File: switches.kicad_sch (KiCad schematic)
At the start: 140 parts

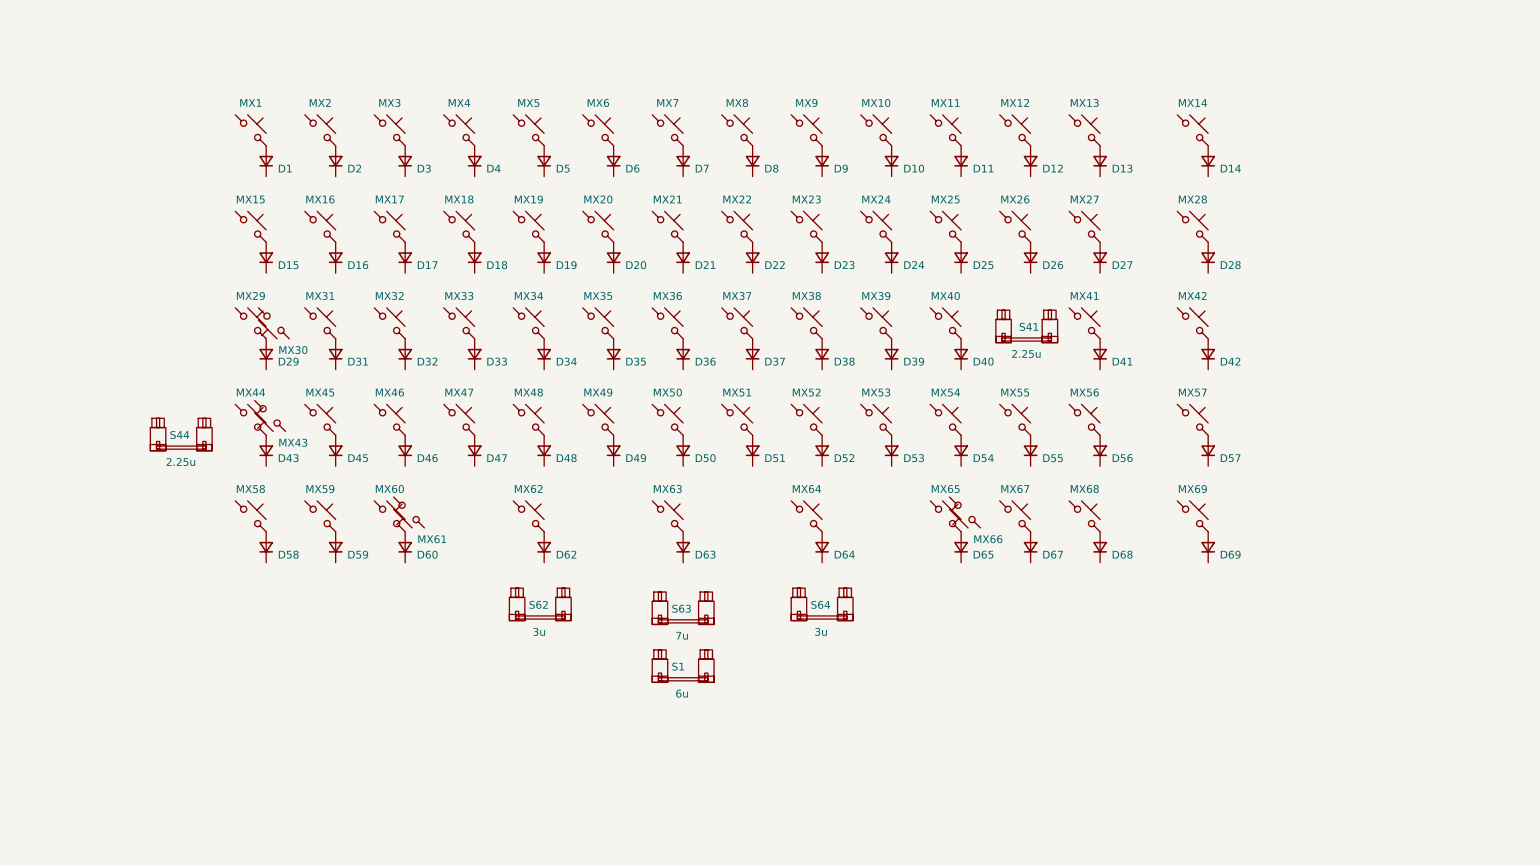
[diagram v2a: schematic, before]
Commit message: Complete matrix and add Skyloong knob module
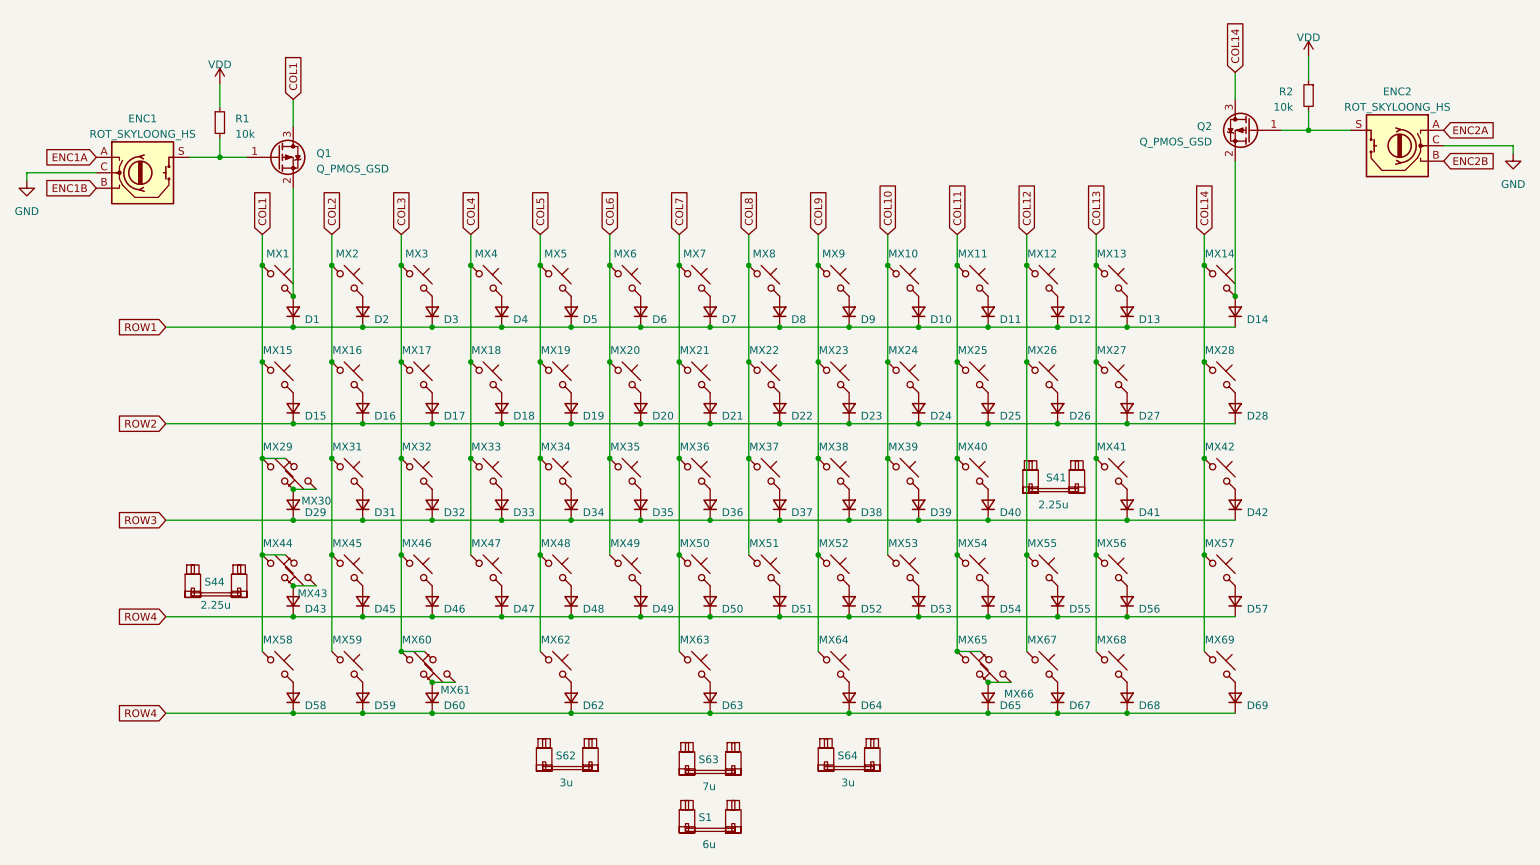
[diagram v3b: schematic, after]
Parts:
- added ENC1, ENC2: ROT_SKYLOONG_HS, PCM_marbastlib-various:ROT_SKYLOONG_HS-Switch, symbol PCM_marbastlib-various:ROT_SKYLOONG_HS-Switch
- added Q1, Q2: Q_PMOS_GSD, Package_TO_SOT_SMD:SOT-23, symbol Device:Q_PMOS_GSD
- added R1, R2: 10k, Resistor_SMD:R_0603_1608Metric, symbol Device:R_Small
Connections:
- net COL14: now reaches MX42.1
- net COL14: now also MX14.1, MX28.1, MX57.1, MX69.1, Q2.3 (D)
- net ROW3: now reaches D35.1 (K)
- net ROW3: now also D29.1 (K), D31.1 (K), D32.1 (K), D33.1 (K), D34.1 (K), D36.1 (K), D37.1 (K), D38.1 (K), D39.1 (K), D40.1 (K), D41.1 (K), D42.1 (K)
- net ROW4: now reaches D52.1 (K)
- net ROW4: now also D43.1 (K), D45.1 (K), D46.1 (K), D47.1 (K), D48.1 (K), D49.1 (K), D50.1 (K), D51.1 (K), D53.1 (K), D54.1 (K), D55.1 (K), D56.1 (K), D57.1 (K), D58.1 (K), D59.1 (K), D60.1 (K), D62.1 (K), D63.1 (K), D64.1 (K), D65.1 (K), D67.1 (K), D68.1 (K), D69.1 (K)
- net ROW1: now reaches D3.1 (K)
- net ROW1: now also D1.1 (K), D10.1 (K), D11.1 (K), D12.1 (K), D13.1 (K), D14.1 (K), D2.1 (K), D4.1 (K), D5.1 (K), D6.1 (K), D7.1 (K), D8.1 (K), D9.1 (K)
- net ROW2: now reaches D15.1 (K)
- net ROW2: now also D16.1 (K), D17.1 (K), D18.1 (K), D19.1 (K), D20.1 (K), D21.1 (K), D22.1 (K), D23.1 (K), D24.1 (K), D25.1 (K), D26.1 (K), D27.1 (K), D28.1 (K)
- net COL3: now reaches MX3.1
- net COL3: now also MX17.1, MX32.1, MX46.1, MX60.1, MX61.2
- net COL10: now reaches MX10.1
- net COL10: now also MX24.1, MX39.1, MX53.1
- net COL2: now reaches MX45.1
- net COL2: now also MX16.1, MX2.1, MX31.1, MX59.1
- net at D14.2 (A), MX14.2: now also Q2.2 (S)
- net COL5: now reaches MX19.1
- net COL5: now also MX34.1, MX48.1, MX5.1, MX62.1
- net at D1.2 (A), MX1.2: now also Q1.2 (S)
- net COL11: now reaches MX11.1
- net COL11: now also MX25.1, MX40.1, MX54.1, MX65.1, MX66.2
- net COL4: now reaches MX18.1
- net COL4: now also MX33.1, MX4.1, MX47.1
- net COL8: now reaches MX22.1
- net COL8: now also MX37.1, MX51.1, MX8.1
- net COL1: now reaches MX1.1
- net COL1: now also MX15.1, MX29.1, MX30.2, MX43.2, MX44.1, MX58.1, Q1.3 (D)
- net COL12: now reaches MX55.1
- net COL12: now also MX12.1, MX26.1, MX67.1
- net COL6: now reaches MX20.1
- net COL6: now also MX35.1, MX49.1, MX6.1
- net COL13: now reaches MX56.1
- net COL13: now also MX13.1, MX27.1, MX41.1, MX68.1
- net at D60.2 (A), MX60.2: now also MX61.1
- net at D65.2 (A), MX65.2: now also MX66.1
- net at MX30.1: now also D29.2 (A), MX29.2
- net at D43.2 (A), MX44.2: now also MX43.1
- net COL9: now reaches MX23.1
- net COL9: now also MX38.1, MX52.1, MX64.1, MX9.1
- net COL7: now reaches MX63.1
- net COL7: now also MX21.1, MX36.1, MX50.1, MX7.1
- new net: ENC1.S, Q1.1 (G), R1.2
- new net: ENC2.S, Q2.1 (G), R2.2
- new net ENC1A: ENC1.A
- new net ENC1B: ENC1.B
- new net ENC2A: ENC2.A
- new net ENC2B: ENC2.B
- new net GND: ENC1.C, ENC2.C
- new net VDD: R1.1, R2.1
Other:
- moved on the sheet: D1, D10, D11, D12, D13, D14, D15, D16, D17, D18, D19, D2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

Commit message: Complete column traces
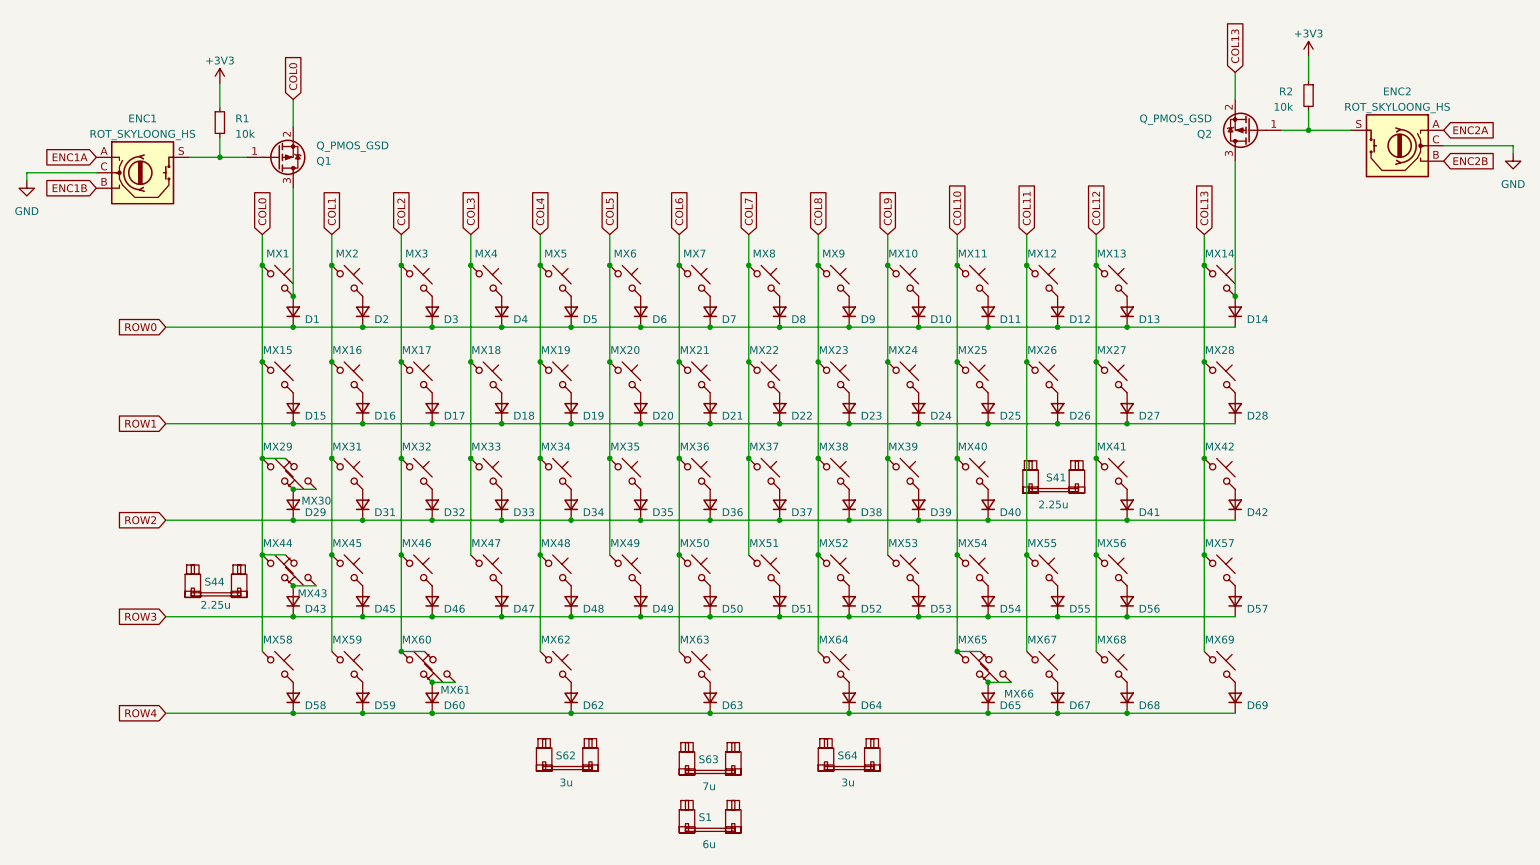
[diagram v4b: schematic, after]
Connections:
- net COL1: now also MX16.1, MX2.1, MX31.1, MX45.1, MX59.1; no longer MX1.1, MX15.1, MX29.1, MX30.2, MX43.2, MX44.1, MX58.1, Q1.3 (D)
- net COL10: now also MX11.1, MX25.1, MX40.1, MX54.1, MX65.1, MX66.2; no longer MX10.1, MX24.1, MX39.1, MX53.1
- net COL11: now also MX12.1, MX26.1, MX55.1, MX67.1; no longer MX11.1, MX25.1, MX40.1, MX54.1, MX65.1, MX66.2
- net COL12: now also MX13.1, MX27.1, MX41.1, MX56.1, MX68.1; no longer MX12.1, MX26.1, MX55.1, MX67.1
- net COL13: now also MX14.1, MX28.1, MX42.1, MX57.1, MX69.1, Q2.2 (S); no longer MX13.1, MX27.1, MX41.1, MX56.1, MX68.1
- net COL2: now also MX17.1, MX3.1, MX32.1, MX46.1, MX60.1, MX61.2; no longer MX16.1, MX2.1, MX31.1, MX45.1, MX59.1
- net COL3: now also MX18.1, MX33.1, MX4.1, MX47.1; no longer MX17.1, MX3.1, MX32.1, MX46.1, MX60.1, MX61.2
- net COL4: now also MX19.1, MX34.1, MX48.1, MX5.1, MX62.1; no longer MX18.1, MX33.1, MX4.1, MX47.1
- net COL5: now also MX20.1, MX35.1, MX49.1, MX6.1; no longer MX19.1, MX34.1, MX48.1, MX5.1, MX62.1
- net COL6: now also MX21.1, MX36.1, MX50.1, MX63.1, MX7.1; no longer MX20.1, MX35.1, MX49.1, MX6.1
- net COL7: now also MX22.1, MX37.1, MX51.1, MX8.1; no longer MX21.1, MX36.1, MX50.1, MX63.1, MX7.1
- net COL8: now also MX23.1, MX38.1, MX52.1, MX64.1, MX9.1; no longer MX22.1, MX37.1, MX51.1, MX8.1
- net COL9: now also MX10.1, MX24.1, MX39.1, MX53.1; no longer MX23.1, MX38.1, MX52.1, MX64.1, MX9.1
- net ROW1: now also D15.1 (K), D16.1 (K), D17.1 (K), D18.1 (K), D19.1 (K), D20.1 (K), D21.1 (K), D22.1 (K), D23.1 (K), D24.1 (K), D25.1 (K), D26.1 (K), D27.1 (K), D28.1 (K); no longer D1.1 (K), D10.1 (K), D11.1 (K), D12.1 (K), D13.1 (K), D14.1 (K), D2.1 (K), D3.1 (K), D4.1 (K), D5.1 (K), D6.1 (K), D7.1 (K), D8.1 (K), D9.1 (K)
- net ROW2: now also D29.1 (K), D31.1 (K), D32.1 (K), D33.1 (K), D34.1 (K), D35.1 (K), D36.1 (K), D37.1 (K), D38.1 (K), D39.1 (K), D40.1 (K), D41.1 (K), D42.1 (K); no longer D15.1 (K), D16.1 (K), D17.1 (K), D18.1 (K), D19.1 (K), D20.1 (K), D21.1 (K), D22.1 (K), D23.1 (K), D24.1 (K), D25.1 (K), D26.1 (K), D27.1 (K), D28.1 (K)
- net ROW3: now also D43.1 (K), D45.1 (K), D46.1 (K), D47.1 (K), D48.1 (K), D49.1 (K), D50.1 (K), D51.1 (K), D52.1 (K), D53.1 (K), D54.1 (K), D55.1 (K), D56.1 (K), D57.1 (K); no longer D29.1 (K), D31.1 (K), D32.1 (K), D33.1 (K), D34.1 (K), D35.1 (K), D36.1 (K), D37.1 (K), D38.1 (K), D39.1 (K), D40.1 (K), D41.1 (K), D42.1 (K)
- net ROW4: no longer D43.1 (K), D45.1 (K), D46.1 (K), D47.1 (K), D48.1 (K), D49.1 (K), D50.1 (K), D51.1 (K), D52.1 (K), D53.1 (K), D54.1 (K), D55.1 (K), D56.1 (K), D57.1 (K)
- net at D14.2 (A), MX14.2: now also Q2.3 (D); no longer Q2.2 (S)
- net at D1.2 (A), MX1.2: now also Q1.3 (D); no longer Q1.2 (S)
- removed net COL14: MX14.1, MX28.1, MX42.1, MX57.1, MX69.1, Q2.3 (D)
- net VDD renamed +3V3
- new net COL0: MX1.1, MX15.1, MX29.1, MX30.2, MX43.2, MX44.1, MX58.1, Q1.2 (S)
- new net ROW0: D1.1 (K), D10.1 (K), D11.1 (K), D12.1 (K), D13.1 (K), D14.1 (K), D2.1 (K), D3.1 (K), D4.1 (K), D5.1 (K), D6.1 (K), D7.1 (K), D8.1 (K), D9.1 (K)
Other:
- moved on the sheet: Q2

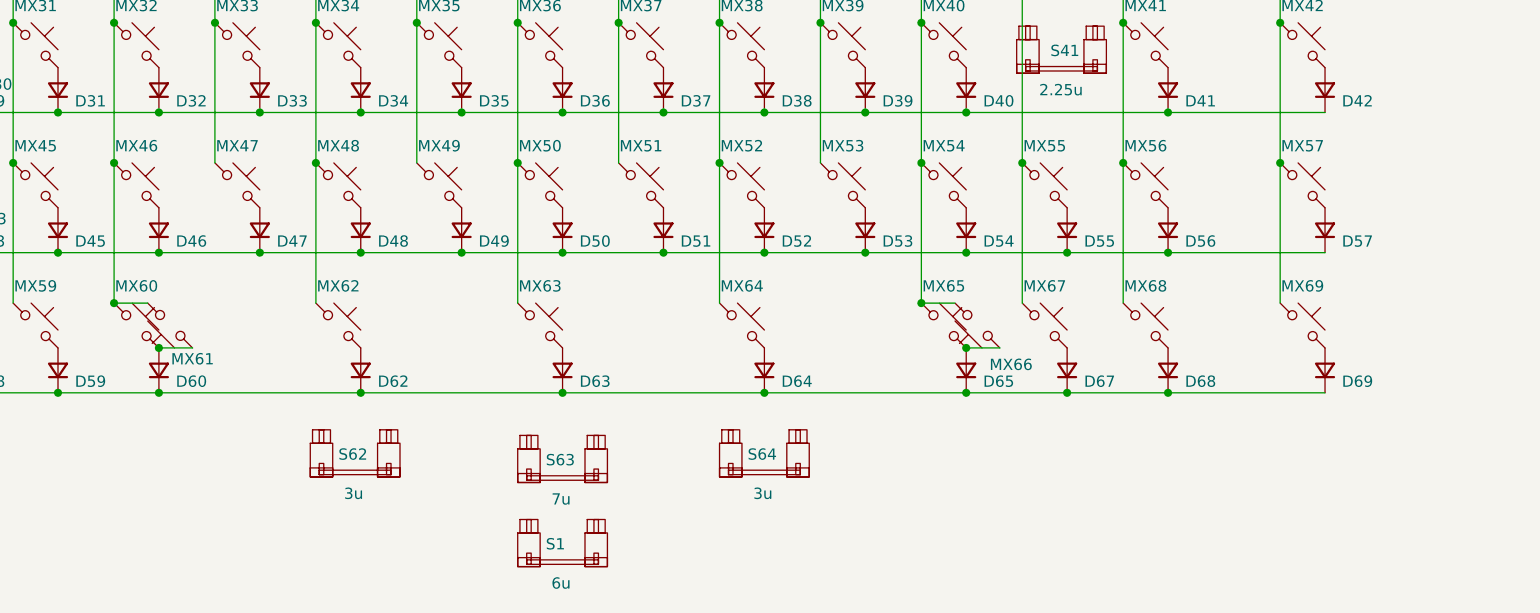
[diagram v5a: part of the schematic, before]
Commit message: Add spacebar 6.25u/2.25u/2.75u and remove 6u/3u/3u
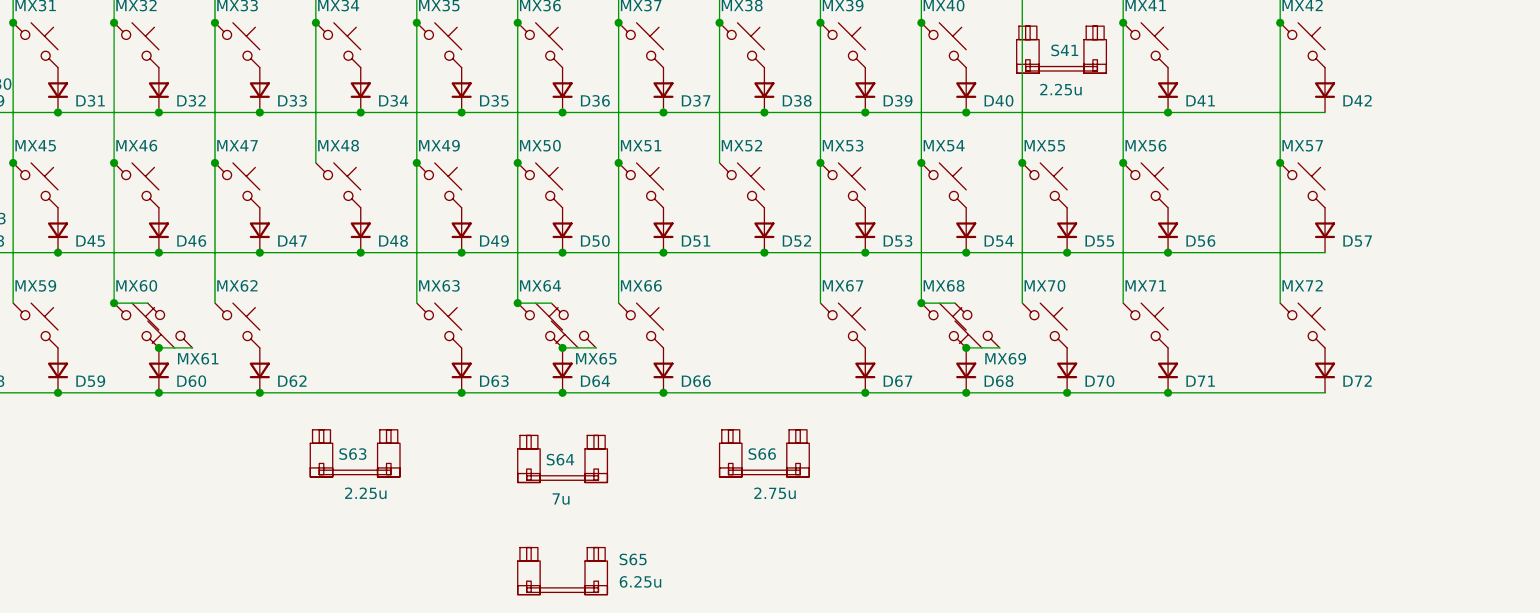
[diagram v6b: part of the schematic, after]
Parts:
- removed MX66: MX_SW_HS, PCM_marbastlib-mx:SW_MX_HS_CPG151101S11_1.5u, symbol PCM_marbastlib-mx:MX_SW_HS_CPG151101S11
- removed S1: 6u, PCM_marbastlib-mx:STAB_MX_P_6u, symbol PCM_marbastlib-mx:MX_stab
- added D62, D67: D_Small, Diode_SMD:D_SOD-123, symbol Device:D_Small
- added MX62, MX65, MX67: MX_SW_HS, PCM_marbastlib-mx:SW_MX_HS_CPG151101S11_1u, symbol PCM_marbastlib-mx:MX_SW_HS_CPG151101S11
- added MX69: MX_SW_HS, PCM_marbastlib-mx:SW_MX_HS_CPG151101S11_1.25u, symbol PCM_marbastlib-mx:MX_SW_HS_CPG151101S11
- added S65: 6.25u, PCM_marbastlib-mx:STAB_MX_P_6.25u, symbol PCM_marbastlib-mx:MX_stab
- MX58: footprint PCM_marbastlib-mx:SW_MX_HS_CPG151101S11_1.5u -> PCM_marbastlib-mx:SW_MX_HS_CPG151101S11_1.25u
- MX60: footprint PCM_marbastlib-mx:SW_MX_HS_CPG151101S11_1u -> PCM_marbastlib-mx:SW_MX_HS_CPG151101S11_1.25u
- MX68: renamed from MX65; footprint PCM_marbastlib-mx:SW_MX_HS_CPG151101S11_1u -> PCM_marbastlib-mx:SW_MX_HS_CPG151101S11_1.75u
- MX71: renamed from MX68; footprint PCM_marbastlib-mx:SW_MX_HS_CPG151101S11_1.5u -> PCM_marbastlib-mx:SW_MX_HS_CPG151101S11_1.25u
- S63: renamed from S62; value 3u -> 2.25u; footprint PCM_marbastlib-mx:STAB_MX_P_3u -> PCM_marbastlib-mx:STAB_MX_P_2.25u
- S66: renamed from S64; value 3u -> 2.75u; footprint PCM_marbastlib-mx:STAB_MX_P_3u -> PCM_marbastlib-mx:STAB_MX_P_2.75u
- renumbered D62 to D63, D63 to D64, D64 to D66, D65 to D68, D67 to D70, D68 to D71, D69 to D72, MX62 to MX63, MX63 to MX64, MX64 to MX66, MX67 to MX70, MX69 to MX72, S63 to S64
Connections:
- net COL10: now also MX69.2
- net COL3: now also MX62.1
- net COL4: no longer MX63.1
- net COL5: now also MX63.1
- net COL6: now also MX65.2
- net COL7: now also MX66.1
- net COL8: no longer MX66.1
- net COL9: now also MX67.1
- net ROW4: now also D62.1 (K), D67.1 (K)
- net at D68.2 (A), MX68.2: now also MX69.1
- net at D64.2 (A), MX64.2: now also MX65.1
- new net: D62.2 (A), MX62.2
- new net: D67.2 (A), MX67.2
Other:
- moved on the sheet: D63, D66, MX63, MX66

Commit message: Swap Backspace and DEL keys
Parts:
- MX26: footprint PCM_marbastlib-mx:SW_MX_HS_CPG151101S11_1.5u -> PCM_marbastlib-mx:SW_MX_HS_CPG151101S11_1u
- MX27: footprint PCM_marbastlib-mx:SW_MX_HS_CPG151101S11_1u -> PCM_marbastlib-mx:SW_MX_HS_CPG151101S11_1.5u
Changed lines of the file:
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@@
 			)
 		)
-		(property "Footprint" "PCM_marbastlib-mx:SW_MX_HS_CPG151101S11_1.5u"
+		(property "Footprint" "PCM_marbastlib-mx:SW_MX_HS_CPG151101S11_1u"
 			(at 195.58 87.63 0)
 			(effects
@@
 			)
 		)
-		(property "Footprint" "PCM_marbastlib-mx:SW_MX_HS_CPG151101S11_1u"
+		(property "Footprint" "PCM_marbastlib-mx:SW_MX_HS_CPG151101S11_1.5u"
 			(at 207.01 87.63 0)
 			(effects
